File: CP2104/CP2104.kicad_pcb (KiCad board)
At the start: 2 copper layers, 15.2 x 20.3 mm, 20 parts, among them J1 Conn_01x06, P1 USB_C_Plug_USB2.0, U1 CP2104

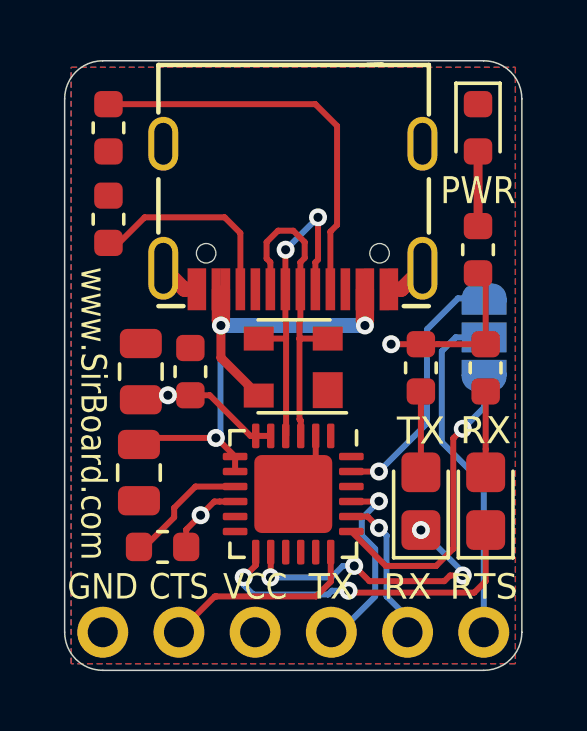
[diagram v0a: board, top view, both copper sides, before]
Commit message: SirUSB Board Revisions
Removed MicroUSB Versions of FT230 and FT231, SolderPaste Layer Adjusted to -0.05mm, Silkscreens optimised, OSHW logo added.
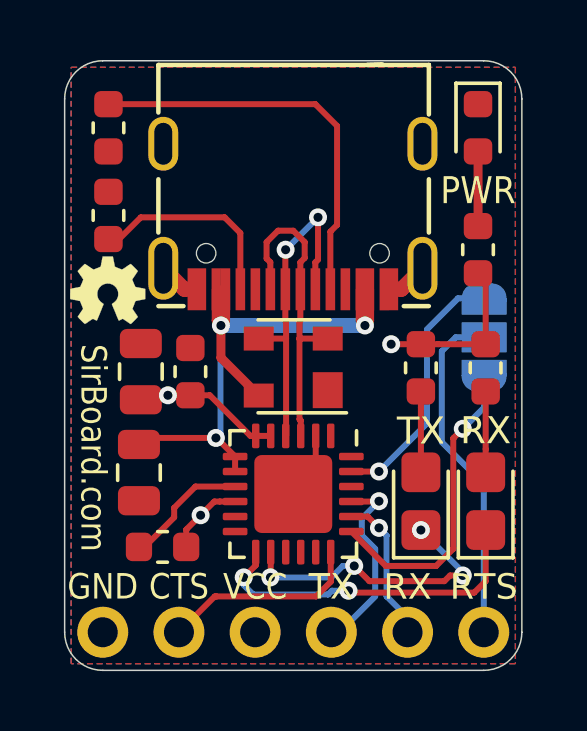
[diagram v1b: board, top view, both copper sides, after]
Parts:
- added G***: LOGO, logo:OSHW36x26, F.Cu at (58.4, 36.7)
- moved R2 0.13 mm to (58.4, 34.2)
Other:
- board text added: "SirBoard.com"
